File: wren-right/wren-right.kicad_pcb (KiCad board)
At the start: 2 copper layers, 151.7 x 117 mm, 61 parts, among them J1 TRRS_Jack, SW0 Reset, U1 ProMicro

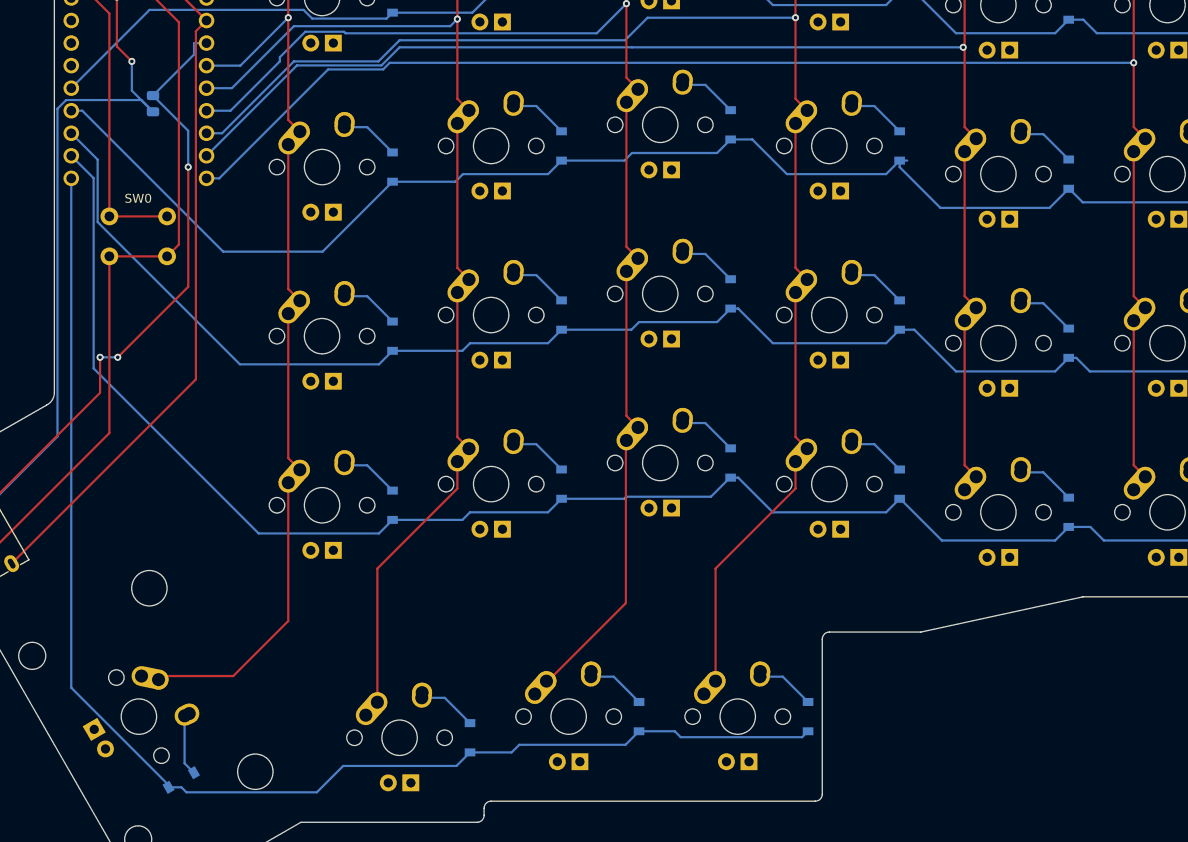
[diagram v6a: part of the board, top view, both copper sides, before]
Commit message: Add PCB Mount Holes
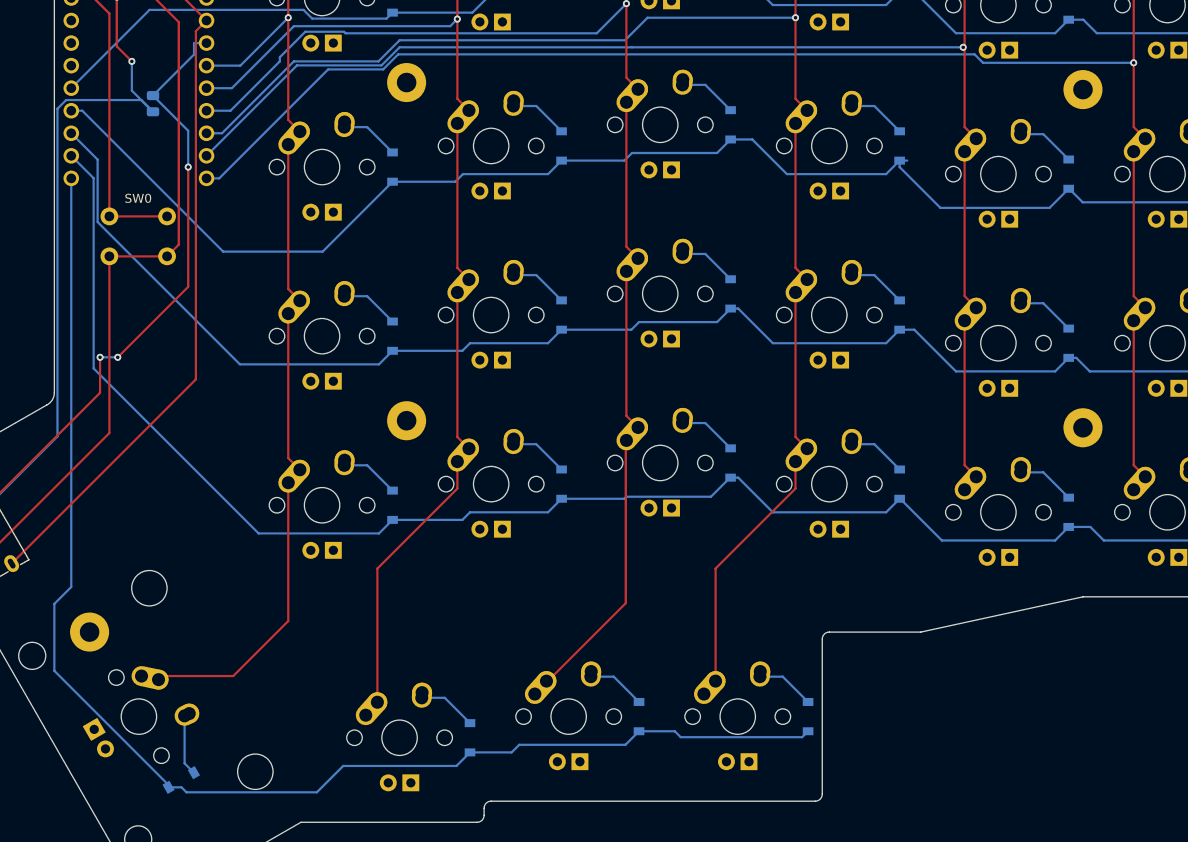
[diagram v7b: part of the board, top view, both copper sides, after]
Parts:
- added REF**: MountingHole_2.2mm_M2_Pad, MountingHole:MountingHole_2.2mm_M2_Pad, F.Cu at (92.0, 127.8)
- added REF**: MountingHole_2.2mm_M2_Pad, MountingHole:MountingHole_2.2mm_M2_Pad, F.Cu at (127.7, 65.9)
- added REF**: MountingHole_2.2mm_M2_Pad, MountingHole:MountingHole_2.2mm_M2_Pad, F.Cu at (127.7, 104.0)
- added REF**: MountingHole_2.2mm_M2_Pad, MountingHole:MountingHole_2.2mm_M2_Pad, F.Cu at (203.9, 104.8)
- added REF**: MountingHole_2.2mm_M2_Pad, MountingHole:MountingHole_2.2mm_M2_Pad, F.Cu at (203.9, 66.7)
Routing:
- net ROW4: track 148.8 -> 150.4 mm
- net COL5: track 164.2 -> 165.0 mm
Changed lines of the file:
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@@
     (thickness 1.6)
     (drawings 39)
-    (tracks 310)
+    (tracks 314)
     (zones 0)
-    (modules 61)
+    (modules 66)
     (nets 53)
   )
@@
     (add_net SDA)
     (add_net VCC)
+  )
+  (module MountingHole:MountingHole_2.2mm_M2_Pad (layer F.Cu)
+    (at 91.96825 127.79375)
+    (descr "Mounting Hole 2.2mm, M2")
+    (tags "mounting hole 2.2mm m2")
+    (attr virtual)
+    (fp_text reference REF** (at 0 -3.2) (layer F.SilkS) hide
+      (effects (font (size 1 1) (thickness 0.15)))
+    )
+    (fp_text value MountingHole_2.2mm_M2_Pad (at 0 3.2) (layer F.Fab) hide
+      (effects (font (size 1 1) (thickness 0.15)))
+    )
+    (fp_text user %R (at 0.3 0) (layer F.Fab) hide
+      (effects (font (size 1 1) (thickness 0.15)))
+    )
+    (fp_circle (center 0 0) (end 2.2 0) (layer Cmts.User) (width 0.15))
+    (fp_circle (center 0 0) (end 2.45 0) (layer F.CrtYd) (width 0.05))
+    (pad 1 thru_hole circle (at 0 0) (size 4.4 4.4) (drill 2.2) (layers *.Cu *.Mask))
+  )
+  (module MountingHole:MountingHole_2.2mm_M2_Pad (layer F.Cu)
+    (at 127.687 65.88125)
+    (descr "Mounting Hole 2.2mm, M2")
+    (tags "mounting hole 2.2mm m2")
+    (attr virtual)
+    (fp_text reference REF** (at 0 -3.2) (layer F.SilkS) hide
+      (effects (font (size 1 1) (thickness 0.15)))
+    )
+    (fp_text value MountingHole_2.2mm_M2_Pad (at 0 3.2) (layer F.Fab) hide
+      (effects (font (size 1 1) (thickness 0.15)))
+    )
+    (fp_text user %R (at 0.3 0) (layer F.Fab) hide
+      (effects (font (size 1 1) (thickness 0.15)))
+    )
+    (fp_circle (center 0 0) (end 2.2 0) (layer Cmts.User) (width 0.15))
+    (fp_circle (center 0 0) (end 2.45 0) (layer F.CrtYd) (width 0.05))
+    (pad 1 thru_hole circle (at 0 0) (size 4.4 4.4) (drill 2.2) (layers *.Cu *.Mask))
+  )
+  (module MountingHole:MountingHole_2.2mm_M2_Pad (layer F.Cu)
+    (at 127.687 103.98125)
+    (descr "Mounting Hole 2.2mm, M2")
+    (tags "mounting hole 2.2mm m2")
+    (attr virtual)
+    (fp_text reference REF** (at 0 -3.2) (layer F.SilkS) hide
+      (effects (font (size 1 1) (thickness 0.15)))
+    )
+    (fp_text value MountingHole_2.2mm_M2_Pad (at 0 3.2) (layer F.Fab) hide
+      (effects (font (size 1 1) (thickness 0.15)))
+    )
+    (fp_text user %R (at 0.3 0) (layer F.Fab) hide
+      (effects (font (size 1 1) (thickness 0.15)))
+    )
+    (fp_circle (center 0 0) (end 2.2 0) (layer Cmts.User) (width 0.15))
+    (fp_circle (center 0 0) (end 2.45 0) (layer F.CrtYd) (width 0.05))
+    (pad 1 thru_hole circle (at 0 0) (size 4.4 4.4) (drill 2.2) (layers *.Cu *.Mask))
+  )
+  (module MountingHole:MountingHole_2.2mm_M2_Pad (layer F.Cu)
+    (at 203.887 104.775)
+    (descr "Mounting Hole 2.2mm, M2")
+    (tags "mounting hole 2.2mm m2")
+    (attr virtual)
+    (fp_text reference REF** (at 0 -3.2) (layer F.SilkS) hide
+      (effects (font (size 1 1) (thickness 0.15)))
+    )
+    (fp_text value MountingHole_2.2mm_M2_Pad (at 0 3.2) (layer F.Fab) hide
+      (effects (font (size 1 1) (thickness 0.15)))
+    )
+    (fp_text user %R (at 0.3 0) (layer F.Fab) hide
+      (effects (font (size 1 1) (thickness 0.15)))
+    )
+    (fp_circle (center 0 0) (end 2.2 0) (layer Cmts.User) (width 0.15))
+    (fp_circle (center 0 0) (end 2.45 0) (layer F.CrtYd) (width 0.05))
+    (pad 1 thru_hole circle (at 0 0) (size 4.4 4.4) (drill 2.2) (layers *.Cu *.Mask))
+  )
+  (module MountingHole:MountingHole_2.2mm_M2_Pad (layer F.Cu)
+    (at 203.887 66.675)
+    (descr "Mounting Hole 2.2mm, M2")
+    (tags "mounting hole 2.2mm m2")
+    (attr virtual)
+    (fp_text reference REF** (at 0 -3.2) (layer F.SilkS) hide
+      (effects (font (size 1 1) (thickness 0.15)))
+    )
+    (fp_text value MountingHole_2.2mm_M2_Pad (at 0 3.2) (layer F.Fab) hide
+      (effects (font (size 1 1) (thickness 0.15)))
+    )
+    (fp_text user %R (at 0.3 0) (layer F.Fab) hide
+      (effects (font (size 1 1) (thickness 0.15)))
+    )
+    (fp_circle (center 0 0) (end 2.2 0) (layer Cmts.User) (width 0.15))
+    (fp_circle (center 0 0) (end 2.45 0) (layer F.CrtYd) (width 0.05))
+    (pad 1 thru_hole circle (at 0 0) (size 4.4 4.4) (drill 2.2) (layers *.Cu *.Mask))
   )
   (module MX_Only:MX-1U (layer F.Cu)
@@
   (segment (start 172.247599 139.637651) (end 172.9165 138.96875) (width 0.25) (layer B.Cu) (net 30))
   (segment (start 157.902 138.96875) (end 158.570901 139.637651) (width 0.25) (layer B.Cu) (net 30))
-  (segment (start 100.866058 145.025451) (end 100.866058 145.2875) (width 0.25) (layer B.Cu) (net 30))
-  (segment (start 89.9045 134.063893) (end 100.866058 145.025451) (width 0.25) (layer B.Cu) (net 30))
-  (segment (start 89.9045 76.67625) (end 89.9045 134.063893) (width 0.25) (layer B.Cu) (net 30))
+  (segment (start 89.9045 122.71375) (end 89.9045 76.67625) (width 0.25) (layer B.Cu) (net 30))
+  (segment (start 87.9995 132.158893) (end 87.9995 124.61875) (width 0.25) (layer B.Cu) (net 30))
+  (segment (start 100.866058 145.025451) (end 87.9995 132.158893) (width 0.25) (layer B.Cu) (net 30))
+  (segment (start 87.9995 124.61875) (end 89.9045 122.71375) (width 0.25) (layer B.Cu) (net 30))
+  (segment (start 100.866058 145.2875) (end 100.866058 145.025451) (width 0.25) (layer B.Cu) (net 30))
   (segment (start 131.9785 135.2) (end 134.8285 138.05) (width 0.25) (layer B.Cu) (net 31))
   (segment (start 129.39325 135.2) (end 131.9785 135.2) (width 0.25) (layer B.Cu) (net 31))
@@
   (segment (start 209.602 108.99) (end 210.912 110.3) (width 0.25) (layer F.Cu) (net 39))
   (segment (start 209.602 92.71) (end 209.602 108.99) (width 0.25) (layer F.Cu) (net 39))
-  (segment (start 105.1445 76.67625) (end 106.57325 76.67625) (width 0.25) (layer B.Cu) (net 39))
-  (segment (start 125.78341 63.65875) (end 209.602 63.65875) (width 0.25) (layer B.Cu) (net 39))
-  (segment (start 125.042142 64.400018) (end 125.78341 63.65875) (width 0.25) (layer B.Cu) (net 39))
-  (segment (start 118.849481 64.400019) (end 125.042142 64.400018) (width 0.25) (layer B.Cu) (net 39))
-  (segment (start 106.57325 76.67625) (end 118.849481 64.400019) (width 0.25) (layer B.Cu) (net 39))
   (via (at 209.602 63.65875) (size 0.8) (drill 0.4) (layers F.Cu B.Cu) (net 39))
   (segment (start 209.602 63.65875) (end 209.602 70.89) (width 0.25) (layer F.Cu) (net 39))
   (segment (start 209.602 54.61) (end 209.602 63.65875) (width 0.25) (layer F.Cu) (net 39))
+  (segment (start 192.630048 63.65875) (end 209.602 63.65875) (width 0.25) (layer B.Cu) (net 39))
+  (segment (start 126.73591 62.70625) (end 191.677548 62.70625) (width 0.25) (layer B.Cu) (net 39))
+  (segment (start 118.849481 64.400019) (end 125.042142 64.400018) (width 0.25) (layer B.Cu) (net 39))
+  (segment (start 106.57325 76.67625) (end 118.849481 64.400019) (width 0.25) (layer B.Cu) (net 39))
+  (segment (start 125.042142 64.400018) (end 126.73591 62.70625) (width 0.25) (layer B.Cu) (net 39))
+  (segment (start 191.677548 62.70625) (end 192.630048 63.65875) (width 0.25) (layer B.Cu) (net 39))
+  (segment (start 105.1445 76.67625) (end 106.57325 76.67625) (width 0.25) (layer B.Cu) (net 39))
   (segment (start 94.92925 56.35625) (end 95.03625 56.24925) (width 0.25) (layer B.Cu) (net 40))
   (segment (start 89.9045 56.35625) (end 94.92925 56.35625) (width 0.25) (layer B.Cu) (net 40))

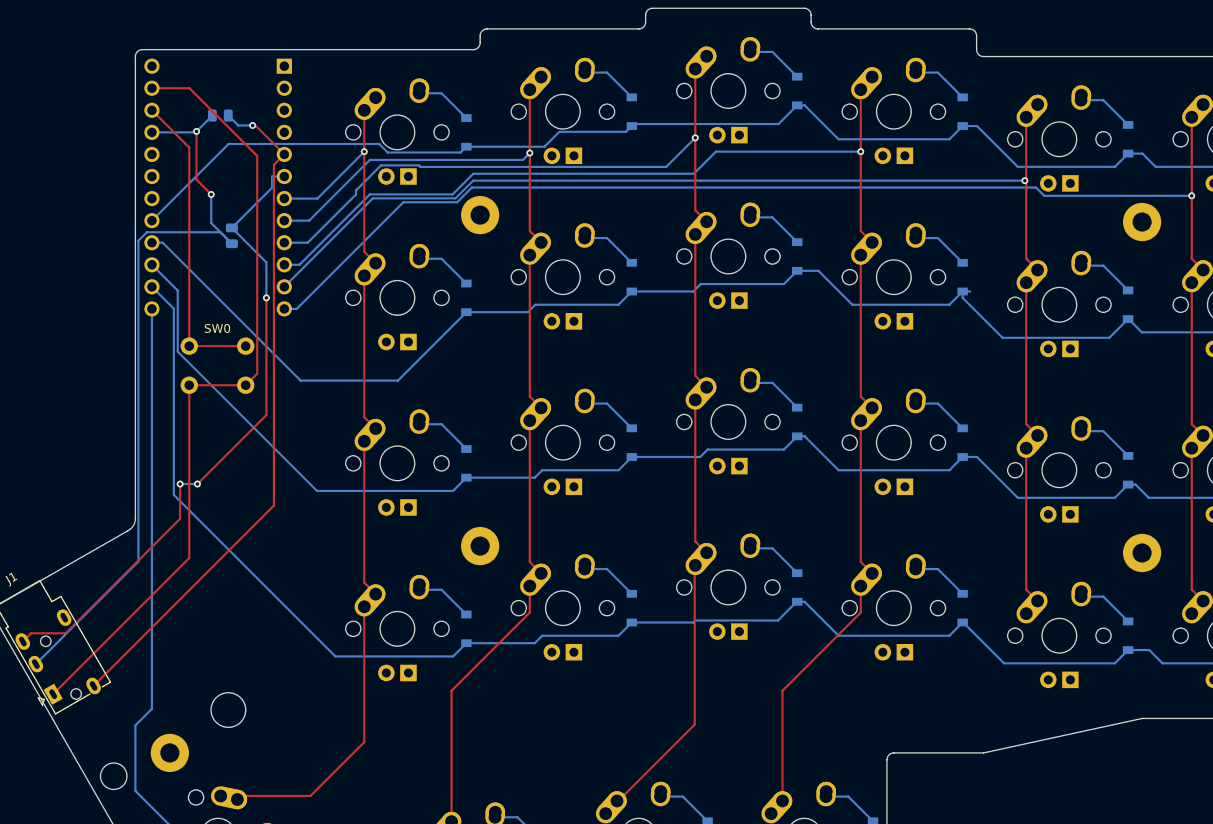
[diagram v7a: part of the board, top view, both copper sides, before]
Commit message: Switch to Elite C Footprints
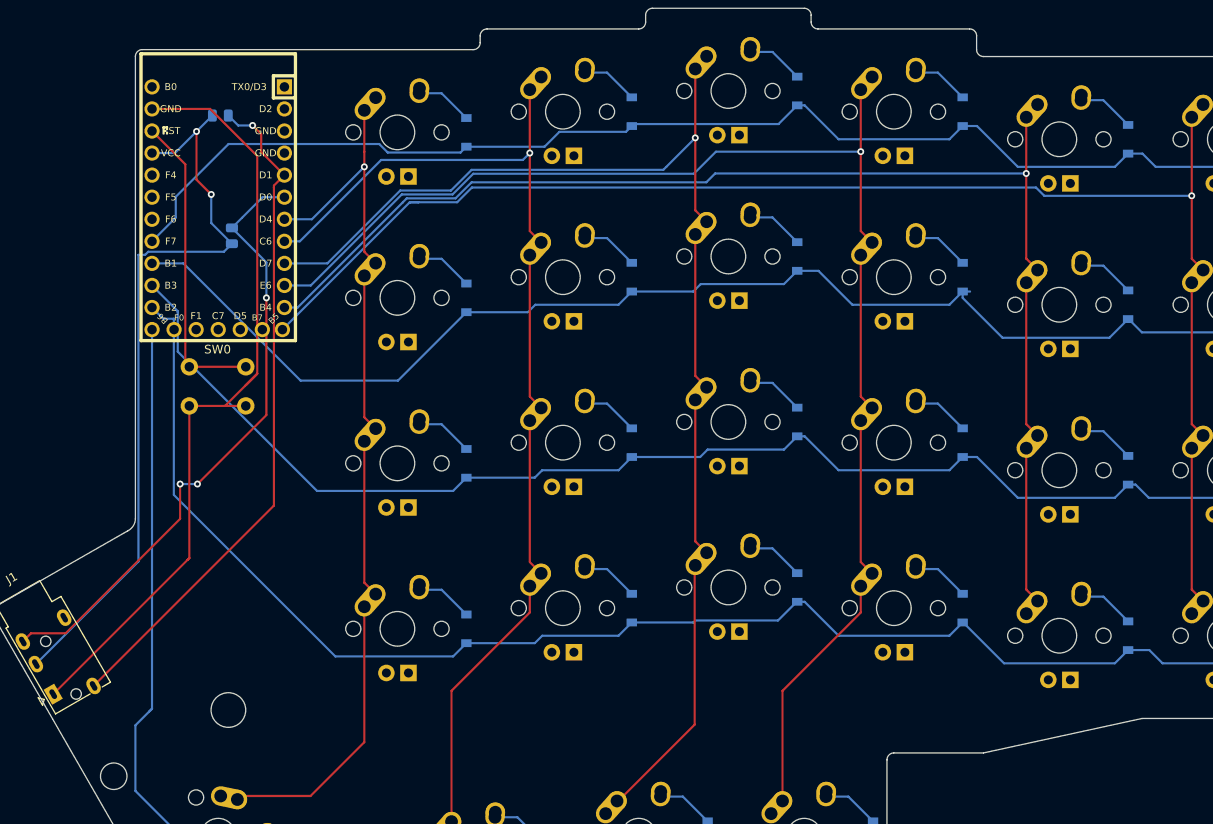
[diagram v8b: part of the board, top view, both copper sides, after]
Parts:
- removed REF** (x5): MountingHole_2.2mm_M2_Pad, MountingHole:MountingHole_2.2mm_M2_Pad
- U1: value ProMicro -> Elite C; footprint footprints:ARDUINO_PRO_MICRO -> footprints:Elite-C
- moved U1 2.38 mm to (97.5, 65.1)
- moved SW0 2.38 mm to (100.7, 83.3)
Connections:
- U1 pad 1: Net-(U1-Pad1) -> (no net)
- U1 pad 18: Net-(U1-Pad18) -> (no net)
- U1 pad 19: Net-(U1-Pad19) -> (no net)
- U1 pad 2: Net-(U1-Pad2) -> (no net)
- U1 pad 20: Net-(U1-Pad20) -> (no net)
- U1 pad 24: Net-(U1-Pad24) -> (no net)
- U1 pad 3: Net-(U1-Pad3) -> (no net)
- U1 pad 4: Net-(U1-Pad4) -> (no net)
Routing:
- net ROW2: track 155.4 -> 153.1 mm
- net ROW0: track 143.8 -> 146.2 mm
- net COL5: track 165.0 -> 167.2 mm
- net GND: track 90.8 -> 92.9 mm
- net ROW4: track 150.4 -> 148.4 mm
- net SCL: track 73.6 -> 71.9 mm
- net ROW3: track 170.3 -> 168.6 mm
- net COL4: track 144.7 -> 146.2 mm
- net ROW1: track 151.1 -> 150.1 mm
- net COL1: track 116.7 -> 117.7 mm
- net COL3: track 154.6 -> 155.6 mm
- net VCC: track 87.7 -> 86.8 mm
- net COL2: track 140.0 -> 140.5 mm
